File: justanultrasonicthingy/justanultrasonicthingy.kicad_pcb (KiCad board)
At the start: 2 copper layers, 5 parts, among them SW1 SW_Push, U1 XIAO-RP2040-DIP, U2 HC-SR04

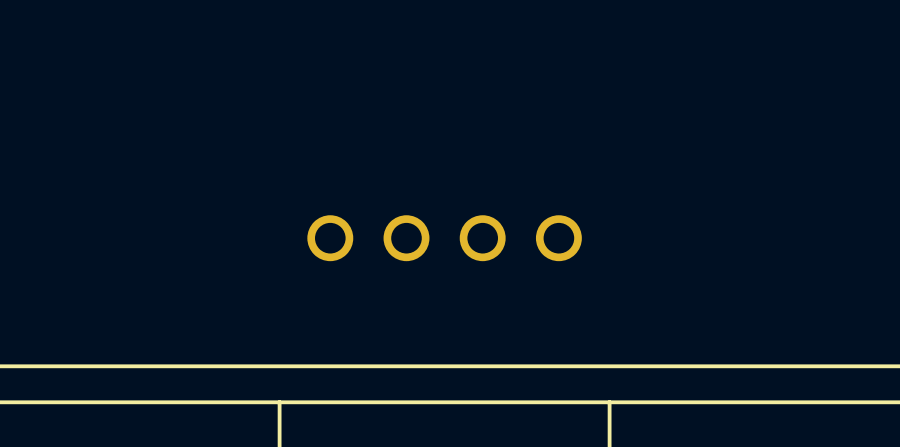
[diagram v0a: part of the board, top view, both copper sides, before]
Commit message: Added Resistors for the components
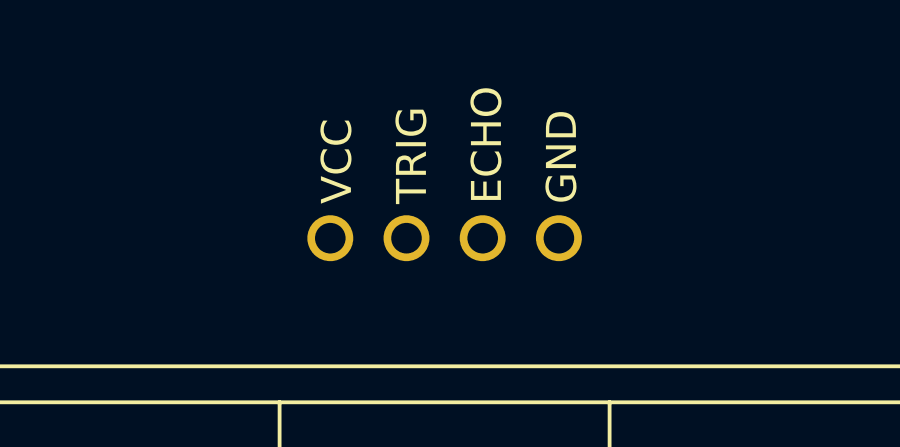
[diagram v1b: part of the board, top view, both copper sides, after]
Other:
- board text added: "ECHO"
- board text added: "TRIG"
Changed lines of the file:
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@@
+		)
+	)
+	(gr_text "ECHO\n"
+		(at 98 32 90)
+		(layer "F.SilkS")
+		(effects
+			(font
+				(size 1 1)
+				(thickness 0.1)
+			)
+			(justify left bottom)
+		)
+	)
+	(gr_text "VCC\n"
+		(at 93 32 90)
+		(layer "F.SilkS")
+		(effects
+			(font
+				(size 1 1)
+				(thickness 0.1)
+			)
+			(justify left bottom)
 		)
 	)
@@
 		(layer "F.SilkS")
 		(effects
+			(font
+				(size 1 1)
+				(thickness 0.1)
+			)
+			(justify left bottom)
+		)
+	)
+	(gr_text "GND\n"
+		(at 100.5 32 90)
+		(layer "F.SilkS")
+		(effects
+			(font
+				(size 1 1)
+				(thickness 0.1)
+			)
+			(justify left bottom)
+		)
+	)
+	(gr_text "TRIG\n"
+		(at 95.5 32 90)
+		(layer "F.SilkS")
+		(effects
